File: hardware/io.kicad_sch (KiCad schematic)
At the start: 9 parts, among them J13 DIN-5_180degree, J14 Mini-DIN-6, J15 COM1, J16 COM2, J17 LPT

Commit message: updates
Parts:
- C1, C2: footprint (none) -> Capacitor_SMD:C_0603_1608Metric
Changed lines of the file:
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@@
       (effects (font (size 1.27 1.27)) (justify left))
     )
-    (property "Footprint" "" (at 72.0852 76.2 0)
+    (property "Footprint" "Capacitor_SMD:C_0603_1608Metric" (at 72.0852 76.2 0)
       (effects (font (size 1.27 1.27)) hide)
     )
@@
       (effects (font (size 1.27 1.27)) (justify left))
     )
-    (property "Footprint" "" (at 72.0852 45.72 0)
+    (property "Footprint" "Capacitor_SMD:C_0603_1608Metric" (at 72.0852 45.72 0)
       (effects (font (size 1.27 1.27)) hide)
     )

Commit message: updates
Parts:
- added C5: C_Polarized_Small_US, symbol Device:C_Polarized_Small_US
- added C6: .1uF, symbol Device:C_Small
- added U20: 68681, Package_DIP:DIP-40_W15.24mm, symbol Interface:68681
- added U21: ATmega8-16A, Package_QFP:TQFP-32_7x7mm_P0.8mm, symbol MCU_Microchip_ATmega:ATmega8-16A
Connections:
- net +5V: now also C6.1, U21.18 (AVCC), U21.4 (VCC), U21.6 (VCC)
- net GND: now also C6.2, U21.21 (AGND), U21.3 (GND), U21.5 (GND)
- new net A0: U21.23 (PC0)
- new net A1: U21.24 (PC1)
- new net A2: U21.25 (PC2)
- new net D0: U21.12 (PB0)
- new net D1: U21.13 (PB1)
- new net D2: U21.14 (PB2)
- new net D3: U21.15 (PB3)
- new net D4: U21.16 (PB4)
- new net D5: U21.17 (PB5)
- new net D6: U21.7 (PB6/XTAL1)
- new net D7: U21.8 (PB7/XTAL2)
- new net KBD_DATA: U21.11 (PD7)
- new net MOU_DATA: U21.10 (PD6)
- new net R/~{W}: U21.28 (PC5)
- new net nPWR_KBD: U21.26 (PC3)
- new net nPWR_MOU: U21.27 (PC4)
- new net ~{IRQ}: U21.9 (PD5)
- new net ~{PS2_CS}: U21.2 (PD4)
- new net ~{RST}: U21.29 (PC6/~{RESET})
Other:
- moved on the sheet: C2, F2, J14

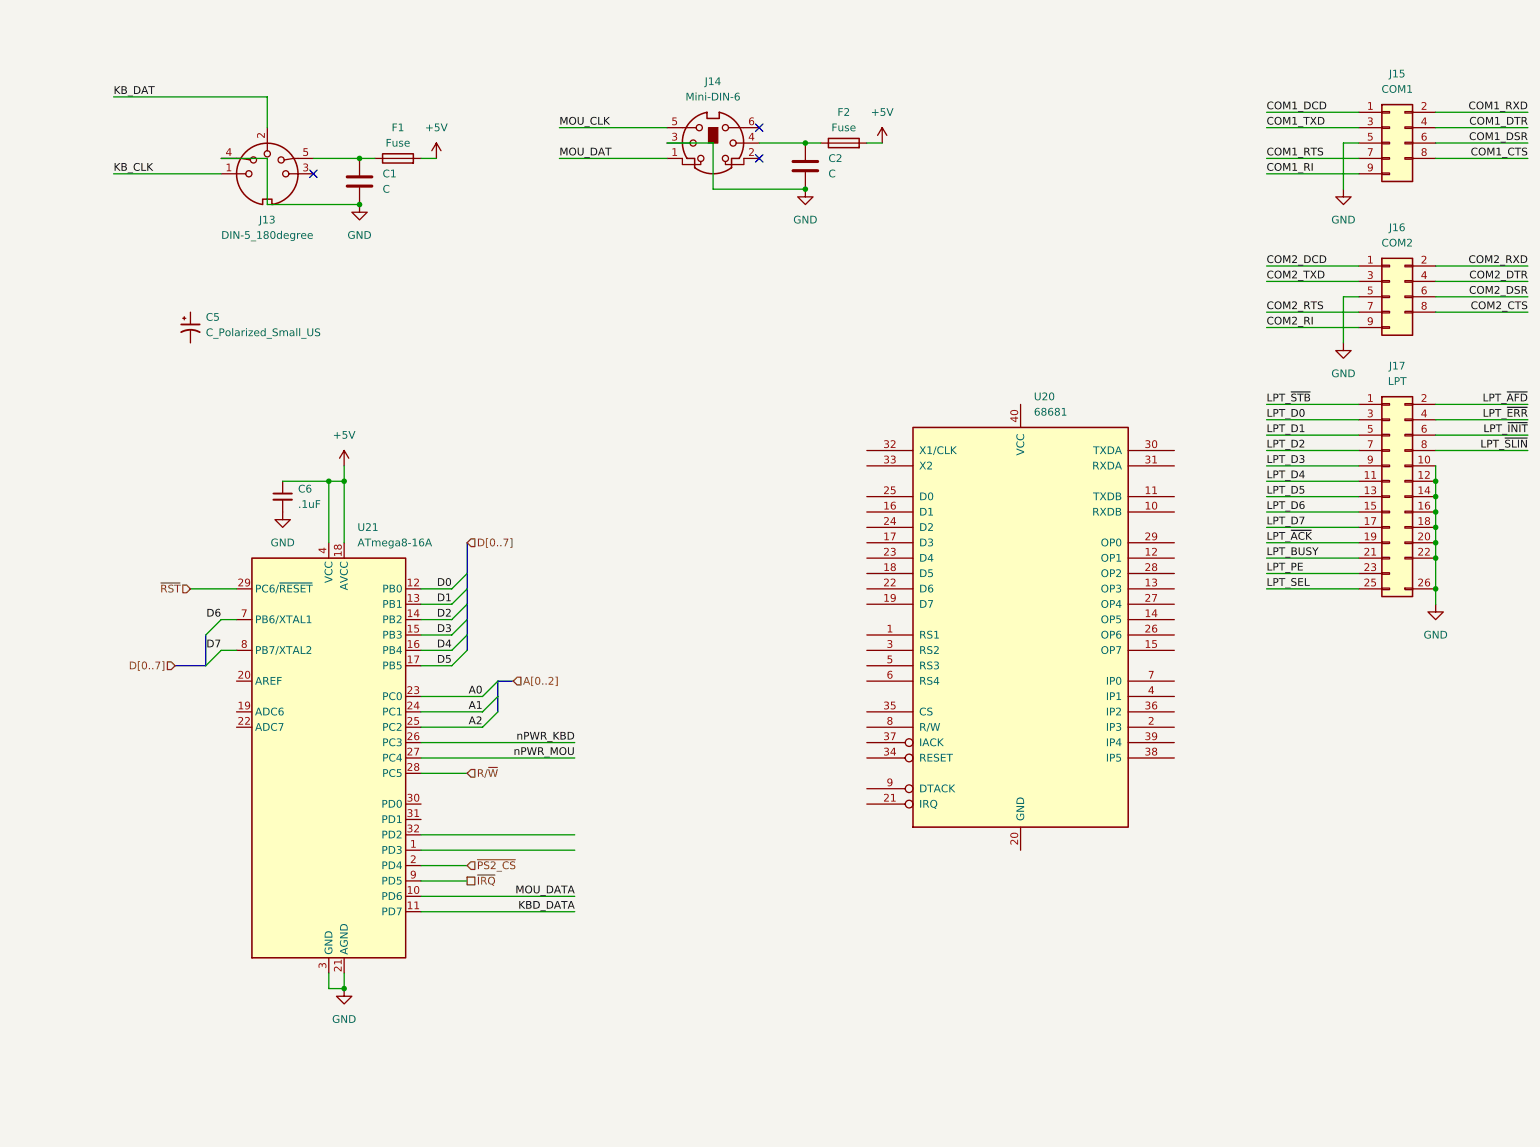
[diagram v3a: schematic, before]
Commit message: add interrupt logic, clean up modules
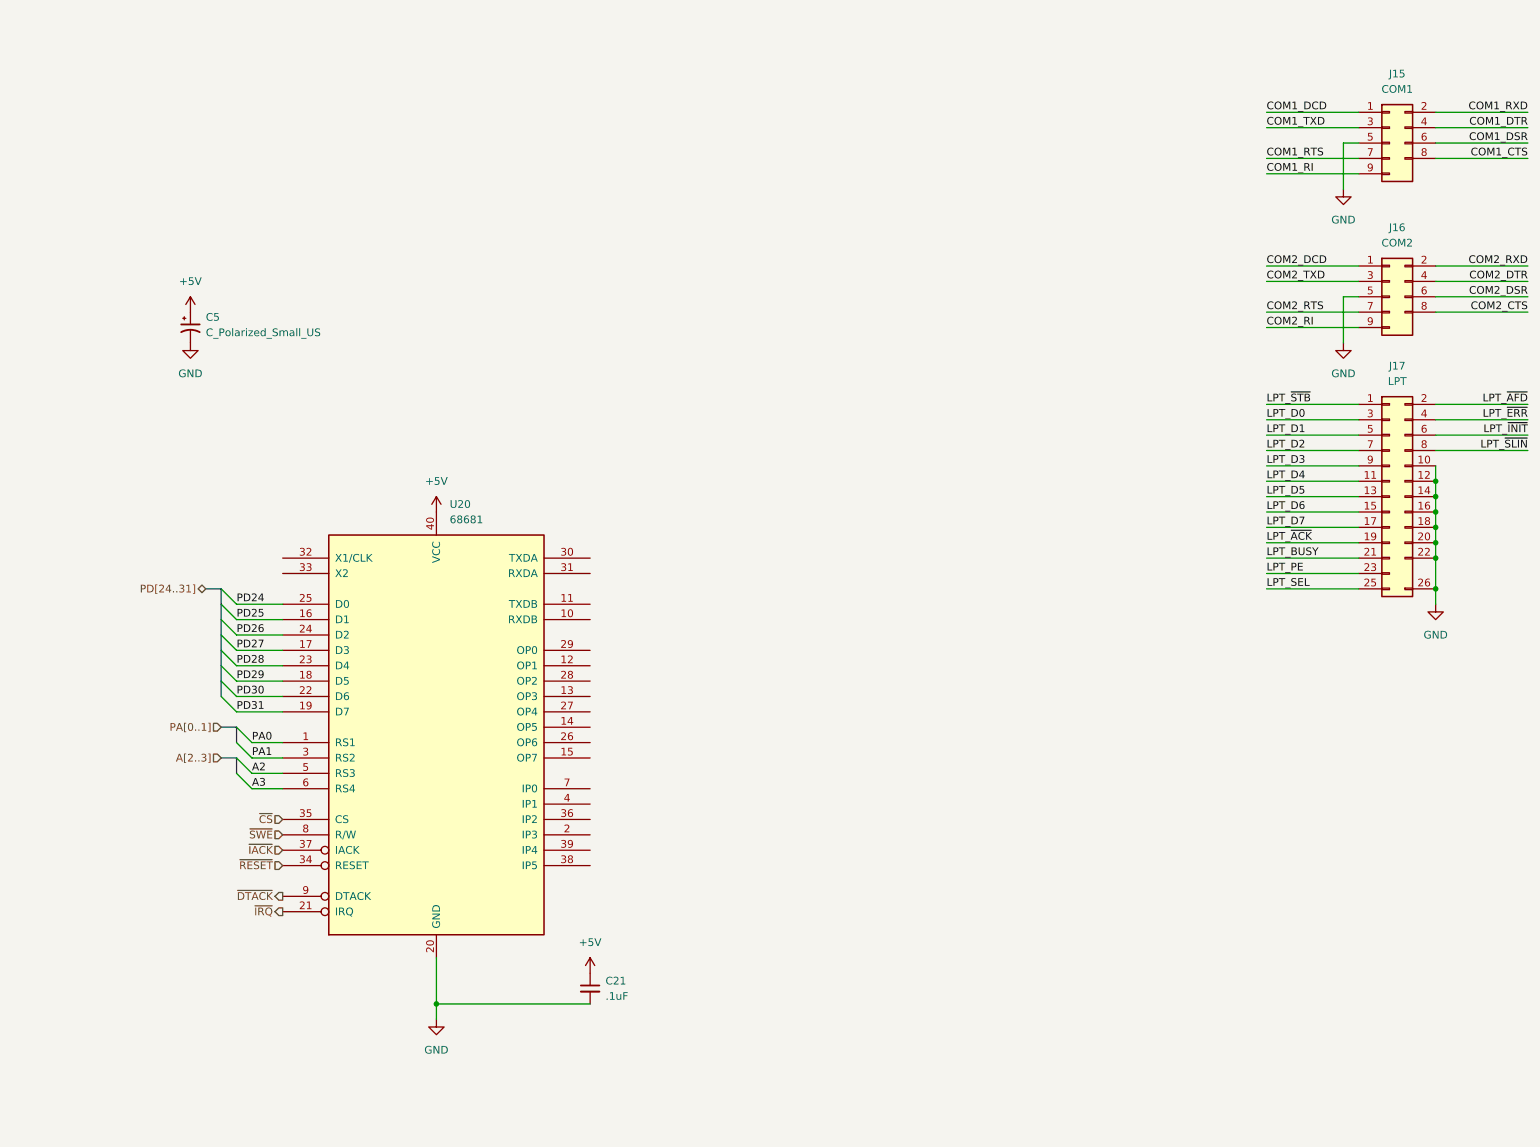
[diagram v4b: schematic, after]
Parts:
- removed C1, C2: C, Capacitor_SMD:C_0603_1608Metric, symbol Device:C
- removed C6: .1uF, symbol Device:C_Small
- removed F1, F2: Fuse, symbol Device:Fuse
- removed J13: DIN-5_180degree, 68040:DIN5-180, symbol Connector:DIN-5_180degree
- removed J14: Mini-DIN-6, 68040:Mini-DIN6, symbol Connector:Mini-DIN-6
- removed U21: ATmega8-16A, Package_QFP:TQFP-32_7x7mm_P0.8mm, symbol MCU_Microchip_ATmega:ATmega8-16A
- added C21: .1uF, symbol Device:C_Small
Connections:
- net +5V: now also C5.1, U20.40 (VCC), C21.1
- net A2: now also U20.5 (RS3)
- net GND: now also C5.2, U20.20 (GND), C21.2
- net ~{IRQ}: now also U20.21 (IRQ)
- net PA0: now reaches U20.1 (RS1)
- net PD25: now reaches U20.16 (D1)
- net PD27: now reaches U20.17 (D3)
- net PD29: now reaches U20.18 (D5)
- net PD31: now reaches U20.19 (D7)
- net PD30: now reaches U20.22 (D6)
- net PD28: now reaches U20.23 (D4)
- net PD26: now reaches U20.24 (D2)
- net PD24: now reaches U20.25 (D0)
- net PA1: now reaches U20.3 (RS2)
- net ~{RESET}: now reaches U20.34 (RESET)
- net ~{CS}: now reaches U20.35 (CS)
- net ~{IACK}: now reaches U20.37 (IACK)
- net A3: now reaches U20.6 (RS4)
- net ~{SWE}: now reaches U20.8 (R/W)
- net ~{DTACK}: now reaches U20.9 (DTACK)
- no-connect marks 3 -> 0
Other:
- moved on the sheet: U20

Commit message: getting closer
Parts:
- added C35, C36, C37, C39: 0.1uF, symbol Device:C_Small
- added C38, C40, C41, C42, C43, C44: 0.47uF, symbol Device:C_Small
- added U31, U32: MAX3241E, symbol 68040:MAX3241E
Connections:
- net +5V: now also C35.1, C36.1, U31.26 (VCC), U32.26 (VCC)
- net COM1_CTS: now also U32.7 (R4IN)
- net COM1_DCD: now also U32.4 (R1IN)
- net COM1_DSR: now also U32.8 (R5IN)
- net COM1_DTR: now also U32.11 (T3OUT)
- net COM1_RI: now also U32.5 (R2IN)
- net COM1_RTS: now also U32.10 (T2OUT)
- net COM1_RXD: now also U32.6 (R3IN)
- net COM1_TXD: now also U32.9 (T1OUT)
- net COM2_CTS: now also U31.7 (R4IN)
- net COM2_DCD: now also U31.4 (R1IN)
- net COM2_DSR: now also U31.8 (R5IN)
- net COM2_DTR: now also U31.11 (T3OUT)
- net COM2_RI: now also U31.5 (R2IN)
- net COM2_RTS: now also U31.10 (T2OUT)
- net COM2_RXD: now also U31.6 (R3IN)
- net COM2_TXD: now also U31.9 (T1OUT)
- net GND: now also C35.2, C36.2, C38.2, C40.2, C43.2, C44.2, U31.23 (~{EN}), U31.25 (GND), U32.23 (~{EN}), U32.25 (GND)
- net B_RX: now reaches U20.10 (RXDB)
- net B_RX: now also U31.17 (R3OUT)
- net B_TX: now reaches U20.11 (TXDB)
- net B_TX: now also U31.14 (T1IN)
- net B_~{RTS}: now reaches U20.12 (OP1)
- net B_~{RTS}: now also U31.13 (T2IN)
- net B_~{DTR}: now reaches U20.13 (OP3)
- net B_~{DTR}: now also U31.12 (T3IN)
- net B_~{RING}: now reaches U20.2 (IP3)
- net B_~{RING}: now also U31.18 (R2OUT)
- net A_~{DTR}: now reaches U20.28 (OP2)
- net A_~{DTR}: now also U32.12 (T3IN)
- net A_~{RTS}: now reaches U20.29 (OP0)
- net A_~{RTS}: now also U32.13 (T2IN)
- net A_TX: now reaches U20.30 (TXDA)
- net A_TX: now also U32.14 (T1IN)
- net A_RX: now reaches U20.31 (RXDA)
- net A_RX: now also U32.17 (R3OUT)
- net A_~{RING}: now reaches U20.36 (IP2)
- net A_~{RING}: now also U32.18 (R2OUT)
- net B_~{CTS}: now reaches U20.4 (IP1)
- net B_~{CTS}: now also U31.16 (R4OUT)
- net A_~{CTS}: now reaches U20.7 (IP0)
- net A_~{CTS}: now also U32.16 (R4OUT)
- new net: C41.1, U31.24 (C1-)
- new net: C41.2, U31.1 (C2+)
- new net: C39.1, U32.28 (C1+)
- new net: C39.2, U32.2 (C2-)
- new net: C44.1, U32.3 (VS-)
- new net: C43.1, U31.3 (VS-)
- new net: C37.1, U31.28 (C1+)
- new net: C37.2, U31.2 (C2-)
- new net: C42.1, U32.24 (C1-)
- new net: C42.2, U32.1 (C2+)
- new net: C40.1, U32.27 (VS+)
- new net: C38.1, U31.27 (VS+)
- new net A_DCD: U32.21 (R1OUTB)
- new net A_RING: U32.20 (R2OUTB)
- new net A_~{DCD}: U32.19 (R1OUT)
- new net A_~{DSR}: U32.15 (R5OUT)
- new net B_DCD: U31.21 (R1OUTB)
- new net B_RING: U31.20 (R2OUTB)
- new net B_~{DCD}: U31.19 (R1OUT)
- new net B_~{DSR}: U31.15 (R5OUT)
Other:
- moved on the sheet: C21, C5, U20
